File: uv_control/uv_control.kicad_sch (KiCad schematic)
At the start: 23 parts, among them J1 Keypad, J2 Safety, J3 Fan, J4 12V Power, J5 Light Power, Q1 BSS138, Q2 BSS138, Q3 IRFS7730-7, U1 L7805, U2 MCP1415

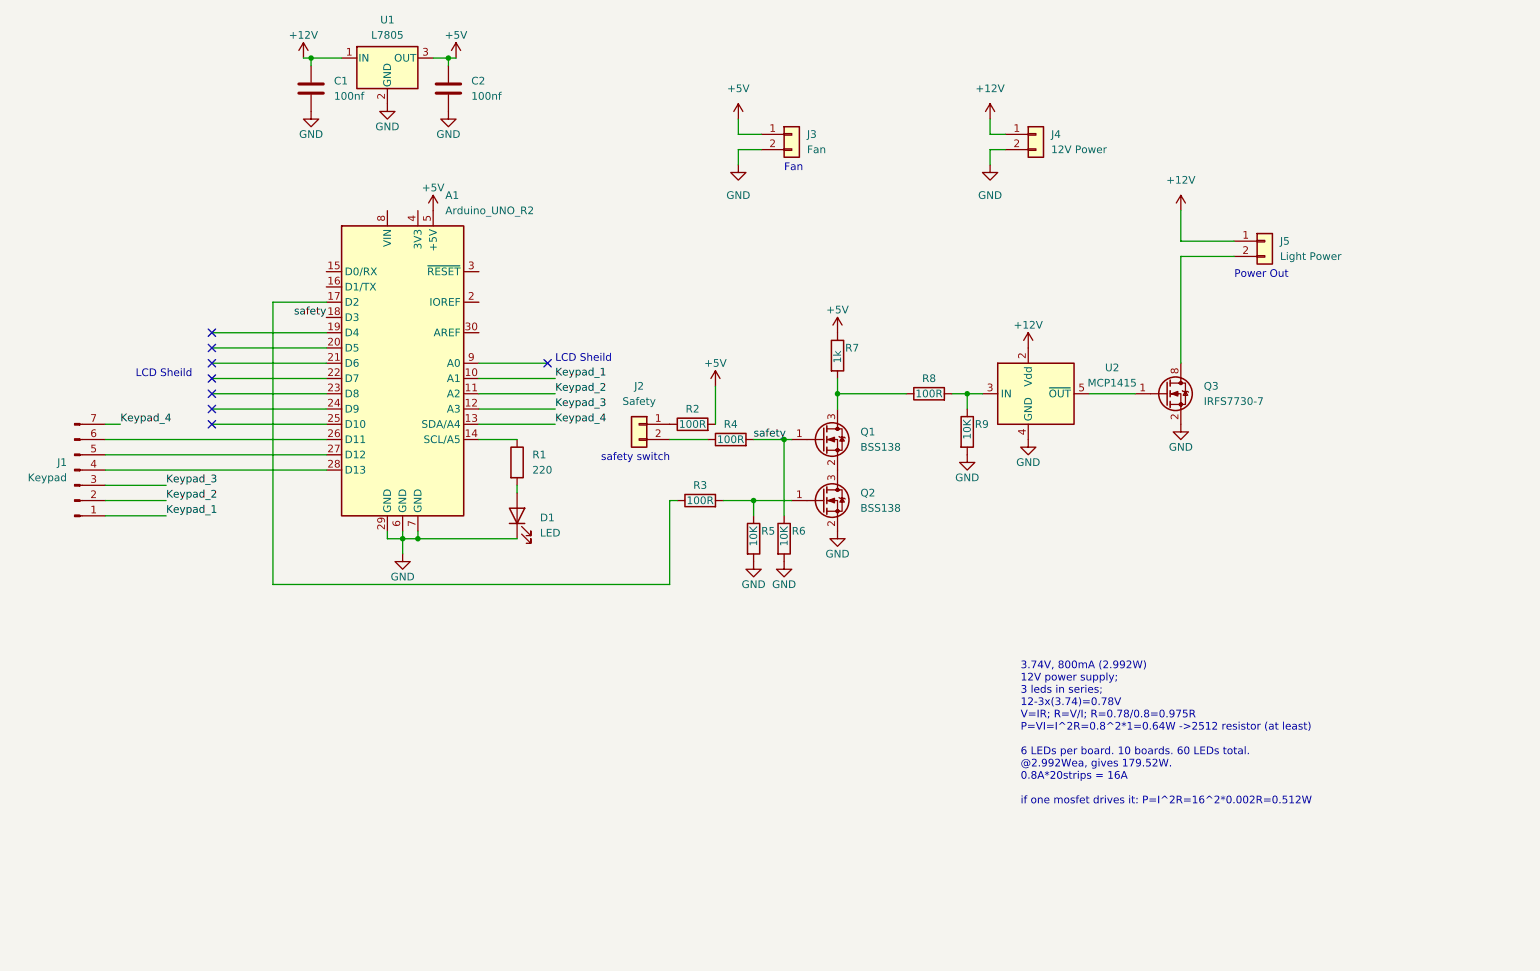
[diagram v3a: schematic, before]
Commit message: Updating PCB to change to 2 layer setup
Added LCD schematic, removing LCD shield design
Fixed XT60 polarity
Added Status LED and Safety LED
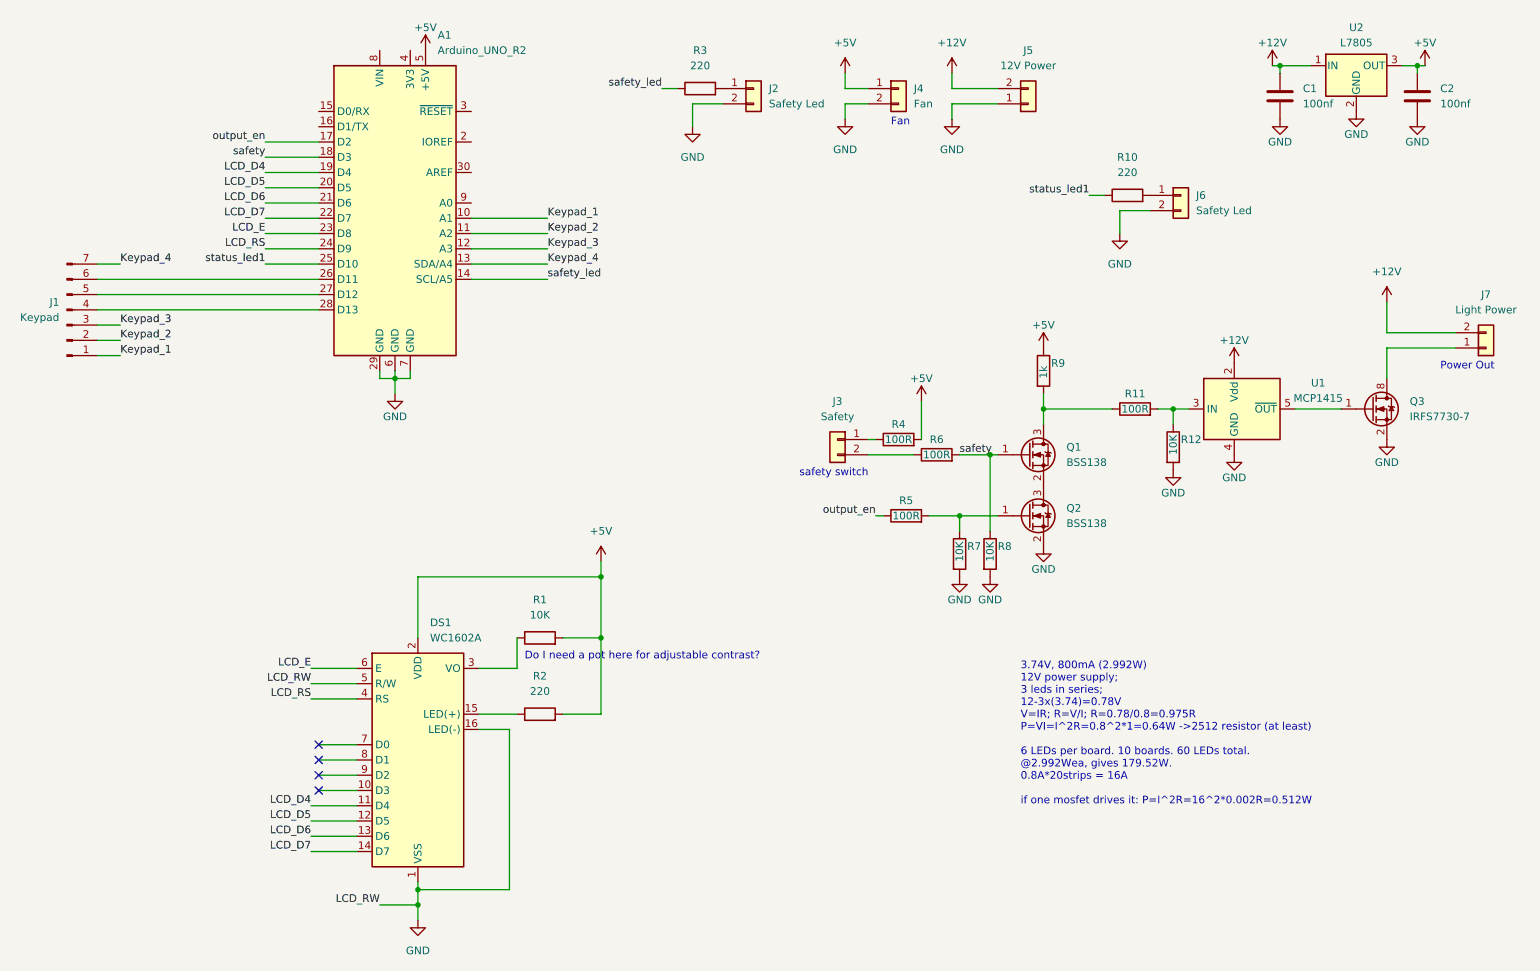
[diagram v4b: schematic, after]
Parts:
- removed D1: LED, symbol Device:LED
- added DS1: WC1602A, Display:WC1602A, symbol Display_Character:WC1602A
- added J2, J6: Safety Led, Connector_JST:JST_EH_B2B-EH-A_1x02_P2.50mm_Vertical, symbol Connector_Generic:Conn_01x02
- added R10, R2, R3: 220, Resistor_SMD:R_0805_2012Metric_Pad1.20x1.40mm_HandSolder, symbol Device:R
- R1: value 220 -> 10K; footprint (none) -> Resistor_SMD:R_0805_2012Metric_Pad1.20x1.40mm_HandSolder
- renumbered J2 to J3, J3 to J4, J4 to J5, J5 to J7, R8 to R11, R9 to R12, R2 to R4, R3 to R5, R4 to R6, R5 to R7, R6 to R8, R7 to R9, U2 to U1, U1 to U2
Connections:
- net +12V: now also J5.2 (Pin_2), J7.2 (Pin_2); no longer J5.1 (Pin_1), J7.1 (Pin_1)
- net +5V: now also R1.2, DS1.2 (VDD), R2.2
- net GND: now also J5.1 (Pin_1), DS1.1 (VSS), DS1.16 (LED(-)), DS1.5 (R/W), J2.2 (Pin_2), J6.2 (Pin_2); no longer J5.2 (Pin_2)
- net at R1.1: now also DS1.3 (VO); no longer A1.14 (SCL/A5)
- net at Q3.8 (D): now also J7.1 (Pin_1); no longer J7.2 (Pin_2)
- net output_en: now reaches A1.17 (D2), R5.1
- net LCD_D4: now reaches A1.19 (D4)
- net LCD_D4: now also DS1.11 (D4)
- net LCD_D5: now reaches A1.20 (D5)
- net LCD_D5: now also DS1.12 (D5)
- net LCD_D6: now reaches A1.21 (D6)
- net LCD_D6: now also DS1.13 (D6)
- net LCD_D7: now reaches A1.22 (D7)
- net LCD_D7: now also DS1.14 (D7)
- net LCD_E: now reaches A1.23 (D8)
- net LCD_E: now also DS1.6 (E)
- net LCD_RS: now reaches A1.24 (D9)
- net LCD_RS: now also DS1.4 (RS)
- net status_led1: now reaches A1.25 (D10)
- net status_led1: now also R10.1
- new net: J6.1 (Pin_1), R10.2
- new net: J2.1 (Pin_1), R3.2
- new net: DS1.15 (LED(+)), R2.1
- new net safety_led: A1.14 (SCL/A5), R3.1
- no-connect marks 8 -> 4
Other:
- note added: "Do I need a pot here for adjustable contrast?"
- note removed: "LCD Sheild"
- moved on the sheet: A1, C1, C2, J1, J3, J4, J5, J7, Q1, Q2, Q3, R11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

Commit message: Reverting to V1 PCB in main branch
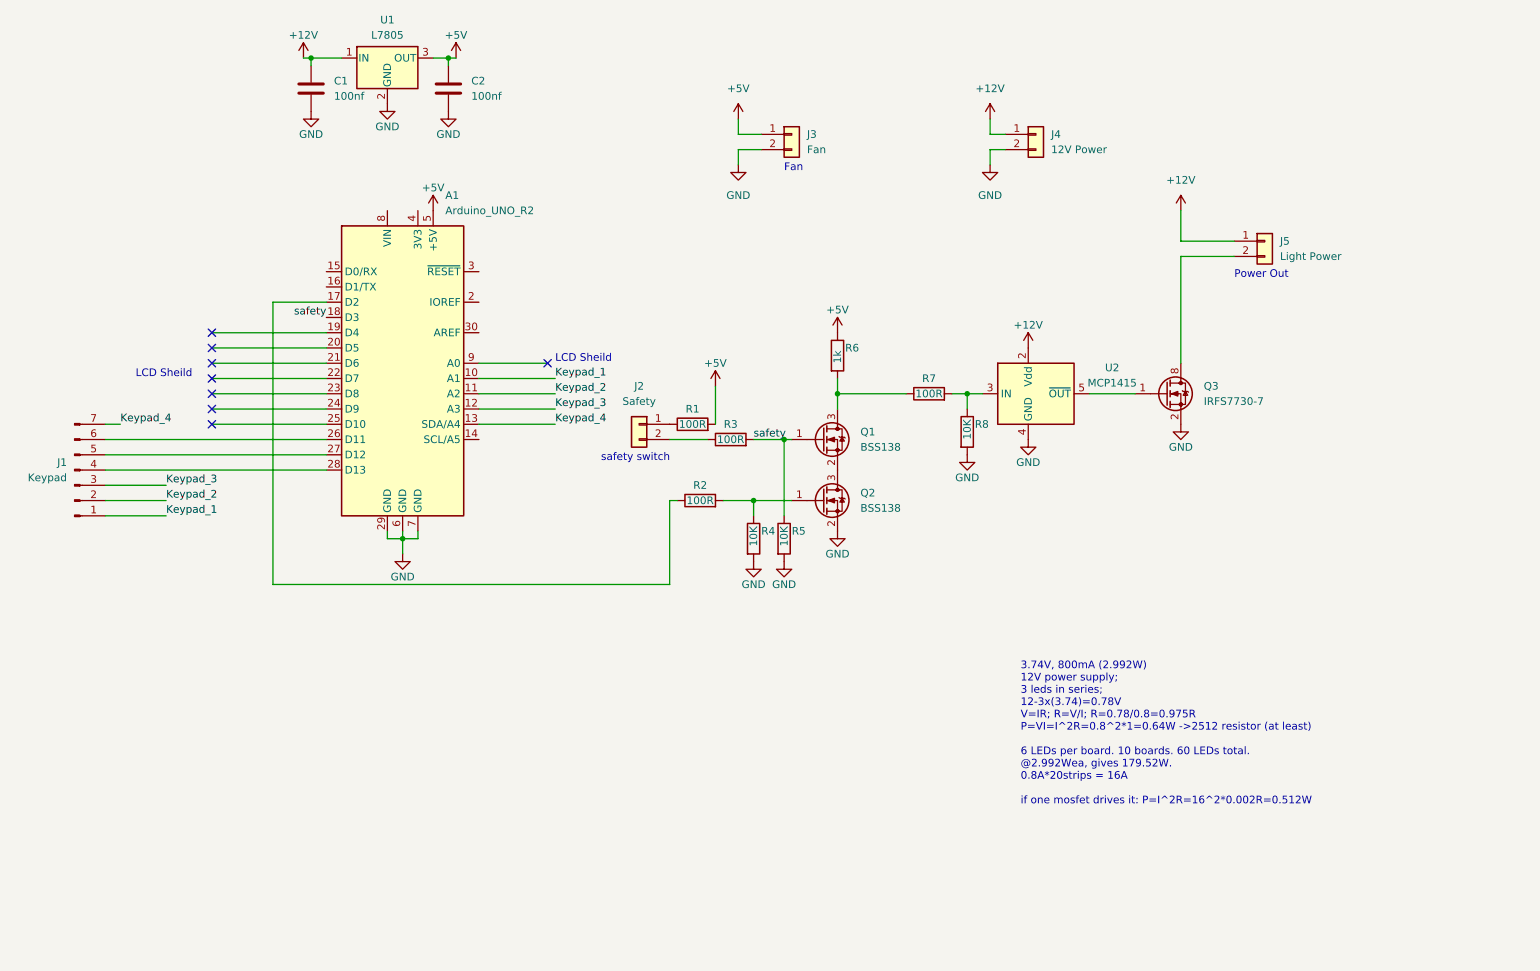
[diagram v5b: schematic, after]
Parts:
- removed DS1: WC1602A, Display:WC1602A, symbol Display_Character:WC1602A
- removed J2, J6: Safety Led, Connector_JST:JST_EH_B2B-EH-A_1x02_P2.50mm_Vertical, symbol Connector_Generic:Conn_01x02
- removed R1: 10K, Resistor_SMD:R_0805_2012Metric_Pad1.20x1.40mm_HandSolder, symbol Device:R
- removed R10, R2, R3: 220, Resistor_SMD:R_0805_2012Metric_Pad1.20x1.40mm_HandSolder, symbol Device:R
- renumbered J3 to J2, J4 to J3, J5 to J4, J7 to J5, R4 to R1, R5 to R2, R6 to R3, R7 to R4, R8 to R5, R9 to R6, R11 to R7, R12 to R8, U2 to U1, U1 to U2
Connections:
- net +12V: now also J4.1 (Pin_1), J5.1 (Pin_1); no longer J4.2 (Pin_2), J5.2 (Pin_2)
- net GND: now also J4.2 (Pin_2); no longer J4.1 (Pin_1)
- net at Q3.8 (D): now also J5.2 (Pin_2); no longer J5.1 (Pin_1)
- net LCD_D4: no longer names the net of A1.19 (D4)
- net LCD_D5: no longer names the net of A1.20 (D5)
- net LCD_D6: no longer names the net of A1.21 (D6)
- net LCD_D7: no longer names the net of A1.22 (D7)
- net LCD_E: no longer names the net of A1.23 (D8)
- net LCD_RS: no longer names the net of A1.24 (D9)
- net output_en: no longer names the net of A1.17 (D2), R2.1
- net safety_led: no longer names the net of A1.14 (SCL/A5)
- net status_led1: no longer names the net of A1.25 (D10)
- no-connect marks 4 -> 8
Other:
- note added: "LCD Sheild"
- note removed: "Do I need a pot here for adjustable contrast?"
- moved on the sheet: A1, C1, C2, J1, J2, J3, J4, J5, Q1, Q2, Q3, R1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
